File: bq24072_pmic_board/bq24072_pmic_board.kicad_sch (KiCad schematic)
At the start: 26 parts, among them J101 USB_B_Micro, J102 Battery, J103 Conn_01x04_Female, U101 BQ24072RGT, U102 AMS1117-3.3

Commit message: WIP
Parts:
- renumbered JP101 to JP1, JP102 to JP2
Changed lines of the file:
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@@
   (symbol (lib_id "Jumper:SolderJumper_2_Open") (at 104.14 57.15 270) (unit 1)
     (in_bom yes) (on_board yes)
-    (property "Reference" "JP102" (id 0) (at 98.425 57.15 0))
+    (property "Reference" "JP2" (id 0) (at 98.425 57.15 0))
     (property "Value" "SolderJumper_2_Open" (id 1) (at 100.7364 57.15 0))
     (property "Footprint" "Jumper:SolderJumper-2_P1.3mm_Open_RoundedPad1.0x1.5mm" (id 2) (at 104.14 57.15 0)
@@
   (symbol (lib_id "Jumper:SolderJumper_2_Open") (at 80.01 71.12 180) (unit 1)
     (in_bom yes) (on_board yes)
-    (property "Reference" "JP101" (id 0) (at 80.01 65.405 0))
+    (property "Reference" "JP1" (id 0) (at 80.01 65.405 0))
     (property "Value" "SolderJumper_2_Open" (id 1) (at 80.01 67.7164 0))
     (property "Footprint" "Jumper:SolderJumper-2_P1.3mm_Open_RoundedPad1.0x1.5mm" (id 2) (at 80.01 71.12 0)
@@
     )
     (path "/9b315454-a4a0-4952-bdbe-d4a8e96c16f9"
-      (reference "JP101") (unit 1) (value "SolderJumper_2_Open") (footprint "Jumper:SolderJumper-2_P1.3mm_Open_RoundedPad1.0x1.5mm")
+      (reference "JP1") (unit 1) (value "SolderJumper_2_Open") (footprint "Jumper:SolderJumper-2_P1.3mm_Open_RoundedPad1.0x1.5mm")
     )
     (path "/61eb7a4f-888e-4082-9c74-1d94f58e7c05"
-      (reference "JP102") (unit 1) (value "SolderJumper_2_Open") (footprint "Jumper:SolderJumper-2_P1.3mm_Open_RoundedPad1.0x1.5mm")
+      (reference "JP2") (unit 1) (value "SolderJumper_2_Open") (footprint "Jumper:SolderJumper-2_P1.3mm_Open_RoundedPad1.0x1.5mm")
     )
     (path "/f879c0e8-5893-4eb4-8e59-2292a632100f"

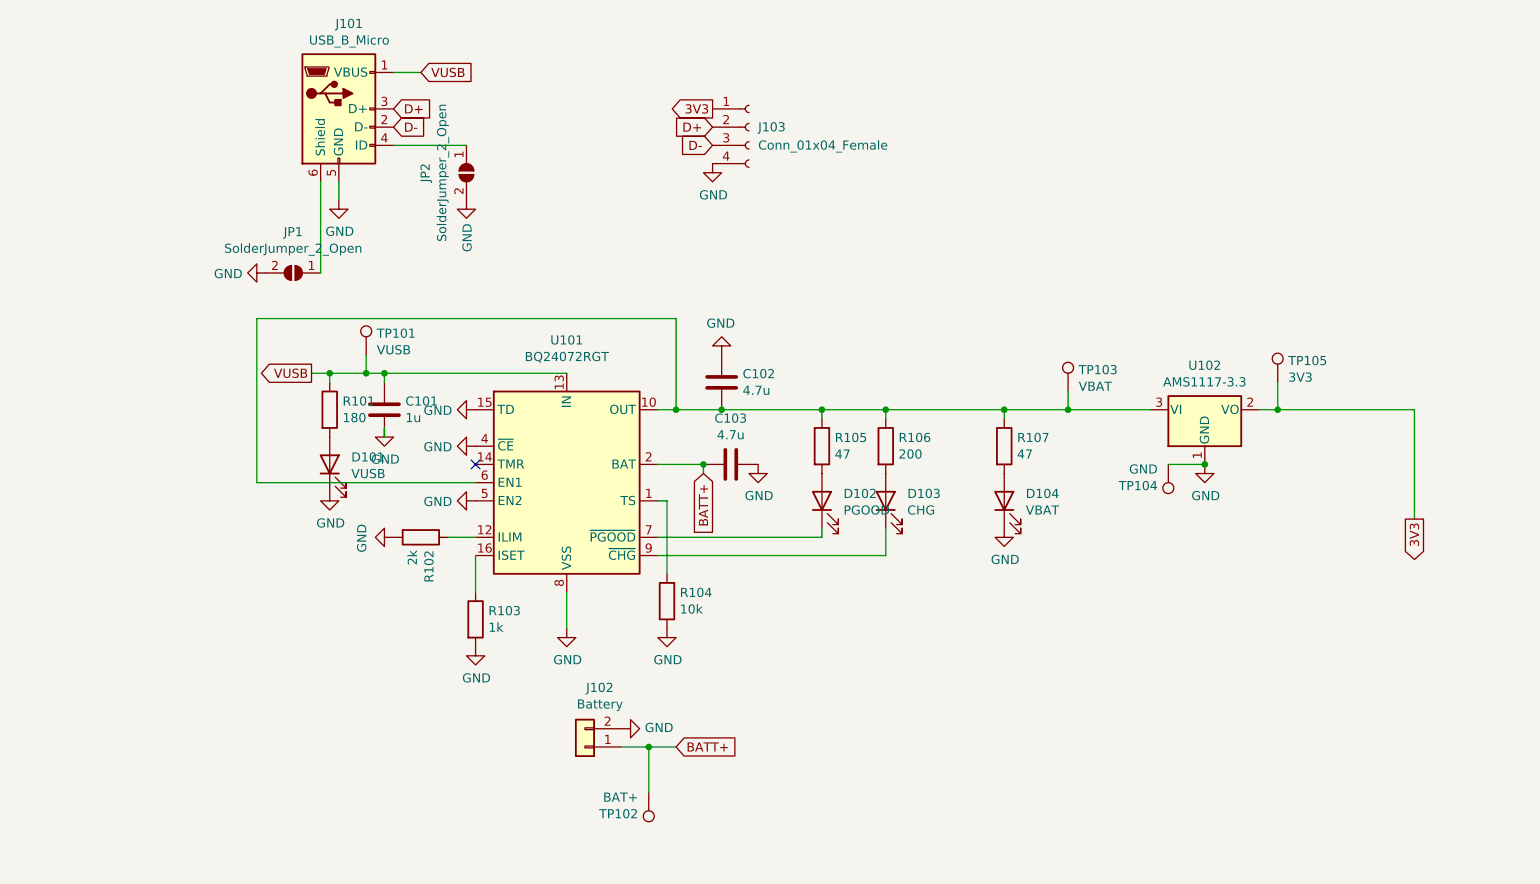
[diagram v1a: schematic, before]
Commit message: [bq24072_pmic_board] Use hierarchical sheet for bq24072
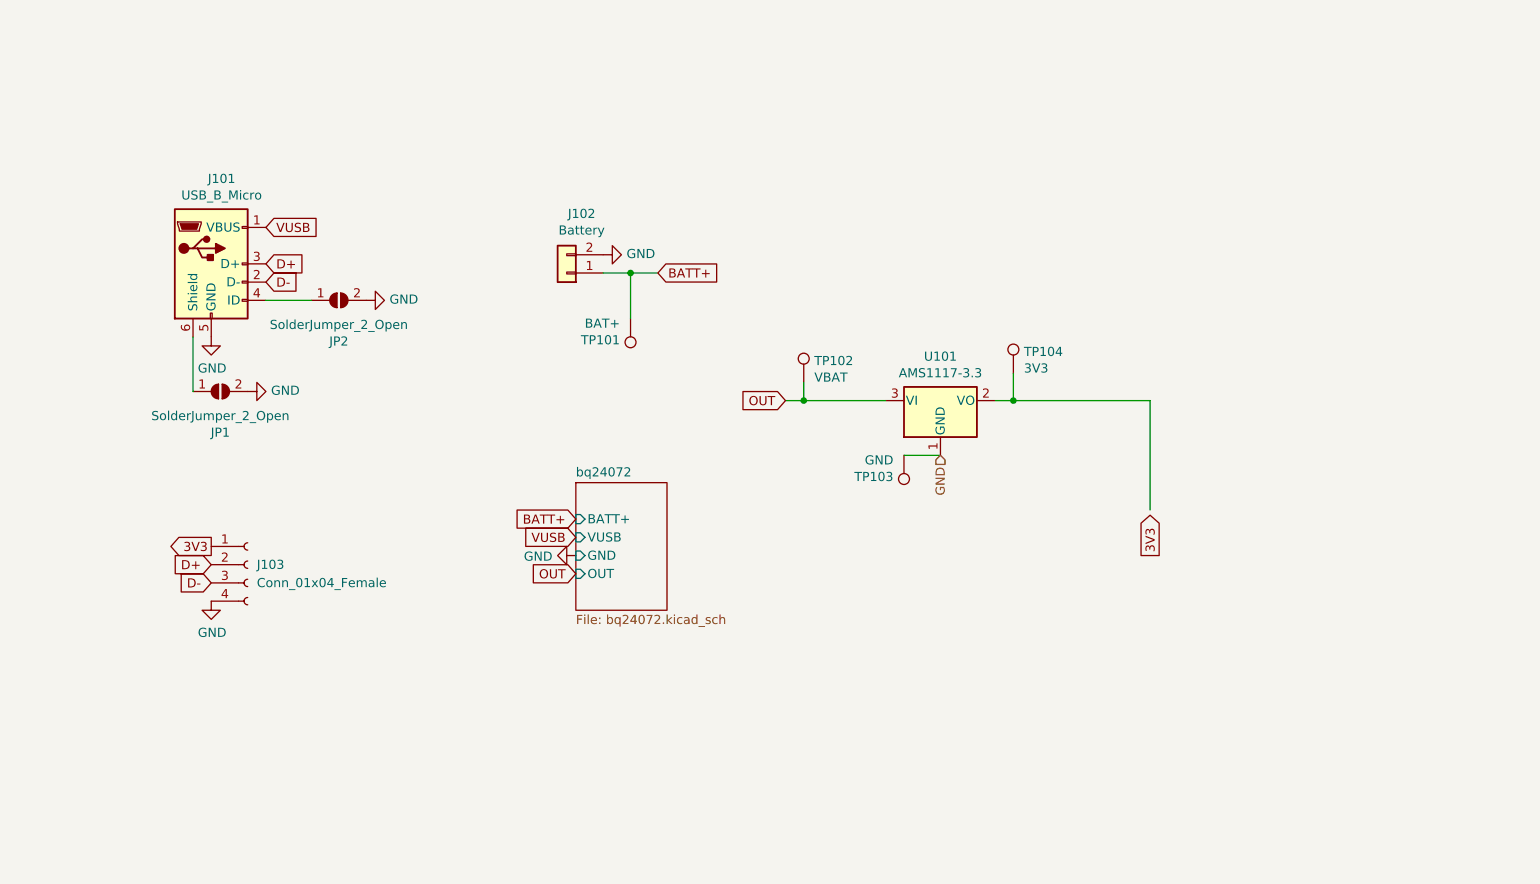
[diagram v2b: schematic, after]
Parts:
- removed C101: 1u, Capacitor_SMD:C_0603_1608Metric, symbol Device:C
- removed C102, C103: 4.7u, Capacitor_SMD:C_0603_1608Metric, symbol Device:C
- removed D101: VUSB, LED_SMD:LED_0603_1608Metric, symbol Device:LED
- removed D102: PGOOD, LED_SMD:LED_0603_1608Metric, symbol Device:LED
- removed D103: CHG, LED_SMD:LED_0805_2012Metric, symbol Device:LED
- removed D104: VBAT, LED_SMD:LED_0603_1608Metric, symbol Device:LED
- removed R101: 180, Resistor_SMD:R_0603_1608Metric, symbol Device:R
- removed R102: 2k, Resistor_SMD:R_0603_1608Metric, symbol Device:R
- removed R103: 1k, Resistor_SMD:R_0603_1608Metric, symbol Device:R
- removed R104: 10k, Resistor_SMD:R_0603_1608Metric, symbol Device:R
- removed R105, R107: 47, Resistor_SMD:R_0603_1608Metric, symbol Device:R
- removed R106: 200, Resistor_SMD:R_0603_1608Metric, symbol Device:R
- removed TP105: 3V3, TestPoint:TestPoint_Pad_D2.0mm, symbol Connector:TestPoint
- removed U101: BQ24072RGT, Package_DFN_QFN:VQFN-16-1EP_3x3mm_P0.5mm_EP1.6x1.6mm, symbol Battery_Management:BQ24072RGT
- removed U102: AMS1117-3.3, Package_TO_SOT_SMD:SOT-223-3_TabPin2, symbol Regulator_Linear:AMS1117-3.3
- added U101: AMS1117-3.3, Package_TO_SOT_SMD:SOT-223-3_TabPin2, symbol Regulator_Linear:AMS1117-3.3
- TP101: value VUSB -> BAT+
- TP102: value BAT+ -> VBAT
- TP103: value VBAT -> GND
- TP104: value GND -> 3V3
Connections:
- net BATT+: now also TP101.1; no longer TP102.1
- net GND: now also TP103.1, U101.1 (GND); no longer TP104.1
- net VUSB: no longer TP101.1
- new net: TP104.1, U101.2 (VO)
- new net OUT: TP102.1, U101.3 (VI)
- no-connect marks 1 -> 0
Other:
- added sheet bq24072 (bq24072.kicad_sch)
- moved on the sheet: J101, J103, JP1, JP2

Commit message: [bq24072_pmic_board] Move some LEDs from the hierarchical sheet
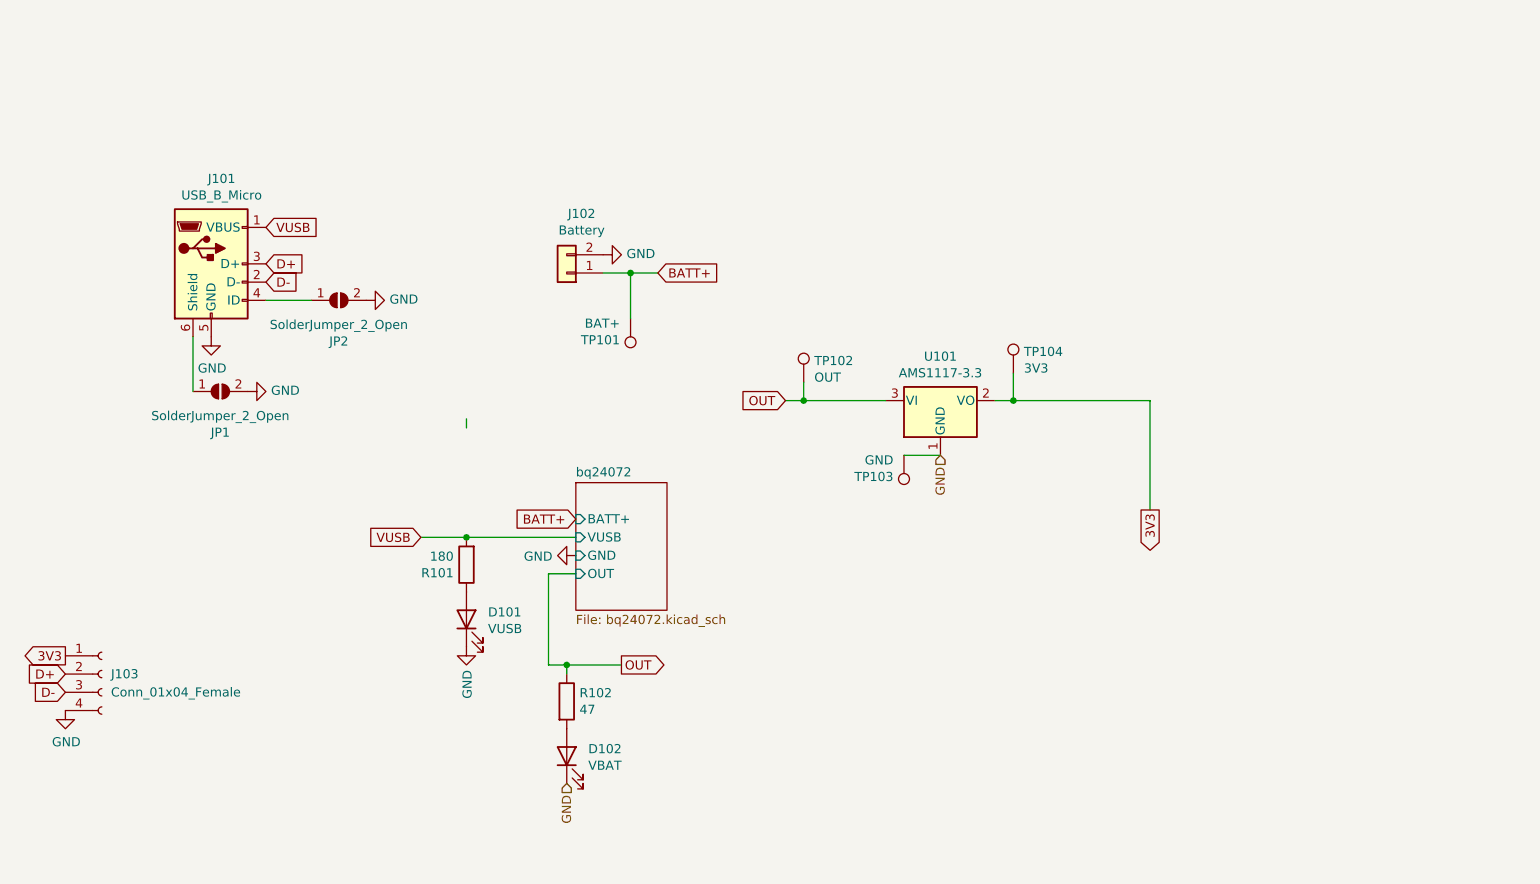
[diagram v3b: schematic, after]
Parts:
- added D101: VUSB, LED_SMD:LED_0603_1608Metric, symbol Device:LED
- added D102: VBAT, LED_SMD:LED_0603_1608Metric, symbol Device:LED
- added R101: 180, Resistor_SMD:R_0603_1608Metric, symbol Device:R
- added R102: 47, Resistor_SMD:R_0603_1608Metric, symbol Device:R
- TP102: value VBAT -> OUT
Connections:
- net 3V3: now also TP104.1, U101.2 (VO)
- net GND: now also D101.1 (K), D102.1 (K)
- net OUT: now also R102.1
- net VUSB: now also R101.2
- new net: D102.2 (A), R102.2
- new net: D101.2 (A), R101.1
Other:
- moved on the sheet: J103

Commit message: [bq24072_pmic_board] Use 1k LED resistors
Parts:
- R101: value 180 -> 1k; LCSC Part C22828 -> C21190
- R102: value 47 -> 1k; LCSC Part C23182 -> C21190
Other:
- note added: "Vf (2.7-3.7) 3.3"
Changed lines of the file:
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@@
   (junction (at 151.13 88.9) (diameter 0) (color 0 0 0 0)
   )
+  (junction (at 170.18 96.52) (diameter 0) (color 0 0 0 0)
+  )
   (junction (at 104.14 107.95) (diameter 0) (color 0 0 0 0)
   )
@@
   (wire (pts (xy 127 77.47) (xy 127 71.12))
     (stroke (width 0) (type default) (color 0 0 0 0))
+  )
+  (text "Vf (2.7-3.7) 3.3" (at 100.33 118.11 270)
+    (effects (font (size 1.27 1.27)) (justify right bottom))
+  )
+  (text "Vf (2.7-3.7) 3.3" (at 128.27 132.08 270)
+    (effects (font (size 1.27 1.27)) (justify right bottom))
   )
   (global_label "D+" (shape input) (at 76.2 69.85 0) (fields_autoplaced)
@@
     )
   )
-  (hierarchical_label "GND" (shape input) (at 170.18 96.52 270)
-    (effects (font (size 1.27 1.27)) (justify right))
-  )
   (hierarchical_label "GND" (shape input) (at 118.11 142.24 270)
     (effects (font (size 1.27 1.27)) (justify right))
@@
     )
     (property "Datasheet" "" (id 3) (at 119.38 110.49 0)
+      (effects (font (size 1.27 1.27)) hide)
+    )
+    (pin "1")
+  )
+  (symbol (lib_id "power:GND") (at 170.18 96.52 0) (unit 1)
+    (in_bom yes) (on_board yes)
+    (property "Reference" "#PWR?" (id 0) (at 170.18 102.87 0)
+      (effects (font (size 1.27 1.27)) hide)
+    )
+    (property "Value" "GND" (id 1) (at 170.307 99.7712 90)
+      (effects (font (size 1.27 1.27)) (justify right))
+    )
+    (property "Footprint" "" (id 2) (at 170.18 96.52 0)
+      (effects (font (size 1.27 1.27)) hide)
+    )
+    (property "Datasheet" "" (id 3) (at 170.18 96.52 0)
       (effects (font (size 1.27 1.27)) hide)
     )
@@
       (effects (font (size 1.27 1.27)) (justify left))
     )
-    (property "Value" "47" (id 1) (at 119.888 131.953 0)
+    (property "Value" "1k" (id 1) (at 119.888 131.953 0)
       (effects (font (size 1.27 1.27)) (justify left))
     )
@@
       (effects (font (size 1.27 1.27)) hide)
     )
-    (property "LCSC Part" "C23182" (id 4) (at 118.11 130.81 0)
+    (property "LCSC Part" "C21190" (id 4) (at 118.11 130.81 0)
       (effects (font (size 1.27 1.27)) hide)
     )
@@
       (effects (font (size 1.27 1.27)) (justify left))
     )
-    (property "Value" "180" (id 1) (at 102.362 110.617 0)
+    (property "Value" "1k" (id 1) (at 102.362 110.617 0)
       (effects (font (size 1.27 1.27)) (justify left))
     )
@@
       (effects (font (size 1.27 1.27)) hide)
     )
-    (property "LCSC Part" "C22828" (id 4) (at 104.14 111.76 0)
+    (property "LCSC Part" "C21190" (id 4) (at 104.14 111.76 0)
       (effects (font (size 1.27 1.27)) hide)
     )
@@
       (reference "#PWR0118") (unit 1) (value "GND") (footprint "")
     )
+    (path "/229c489b-396d-4e85-8644-35545e2653ea"
+      (reference "#PWR?") (unit 1) (value "GND") (footprint "")
+    )
     (path "/38395bfc-58fa-4d48-a8ef-b7c78e8545e9/37acb77a-4142-4275-bc77-22ae33700deb"
       (reference "C201") (unit 1) (value "1u") (footprint "Capacitor_SMD:C_0603_1608Metric")
@@
     )
     (path "/faa6ffcf-90bd-4ebc-954a-2152f7a206af"
-      (reference "R101") (unit 1) (value "180") (footprint "Resistor_SMD:R_0603_1608Metric")
+      (reference "R101") (unit 1) (value "1k") (footprint "Resistor_SMD:R_0603_1608Metric")
     )
     (path "/dfe7236c-fcbb-415b-ad2a-7a38253b1ce3"
-      (reference "R102") (unit 1) (value "47") (footprint "Resistor_SMD:R_0603_1608Metric")
+      (reference "R102") (unit 1) (value "1k") (footprint "Resistor_SMD:R_0603_1608Metric")
     )
     (path "/38395bfc-58fa-4d48-a8ef-b7c78e8545e9/76f2d397-8f3c-4799-a9c5-6ee7cbb8d293"
@@
     )
     (path "/38395bfc-58fa-4d48-a8ef-b7c78e8545e9/09d94f95-f953-476f-83e3-f1c6db04e6b4"
-      (reference "R205") (unit 1) (value "47") (footprint "Resistor_SMD:R_0603_1608Metric")
+      (reference "R205") (unit 1) (value "1k") (footprint "Resistor_SMD:R_0603_1608Metric")
     )
     (path "/38395bfc-58fa-4d48-a8ef-b7c78e8545e9/e8530dea-0420-47e6-8fcf-1fefae5679ea"
-      (reference "R206") (unit 1) (value "200") (footprint "Resistor_SMD:R_0603_1608Metric")
+      (reference "R206") (unit 1) (value "1k") (footprint "Resistor_SMD:R_0603_1608Metric")
     )
     (path "/6a9c45ce-3ce1-4198-a85d-be194c835774"

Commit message: final touches + v1 jlcpcb fab files
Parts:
- added TP105: VUSB, TestPoint:TestPoint_Pad_D2.0mm, symbol Connector:TestPoint
- D102: value VBAT -> OUT
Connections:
- net VUSB: now also TP105.1
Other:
- note removed: "Vf (2.7-3.7) 3.3"
- moved on the sheet: D101, D102, J101, J102, J103, JP1, JP2, R101, R102, TP101, TP102, TP103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
